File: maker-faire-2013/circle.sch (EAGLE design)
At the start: 11 parts, among them Q1 2N3904, Q2 2N3904

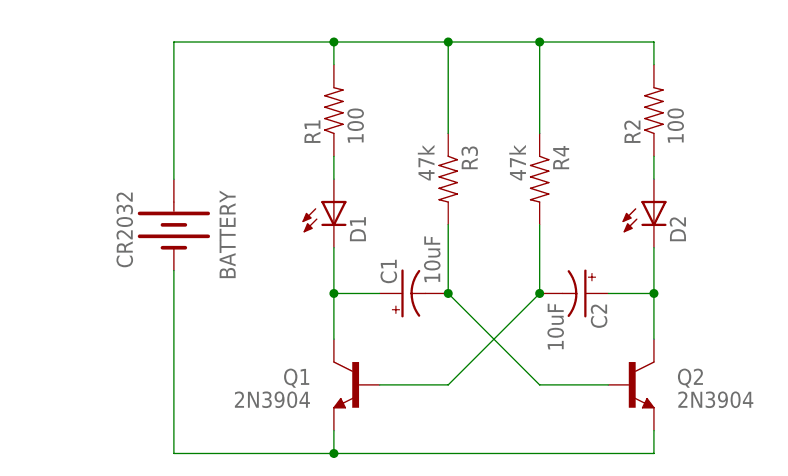
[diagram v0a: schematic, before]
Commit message: Updated with 0.2" caps and power switch
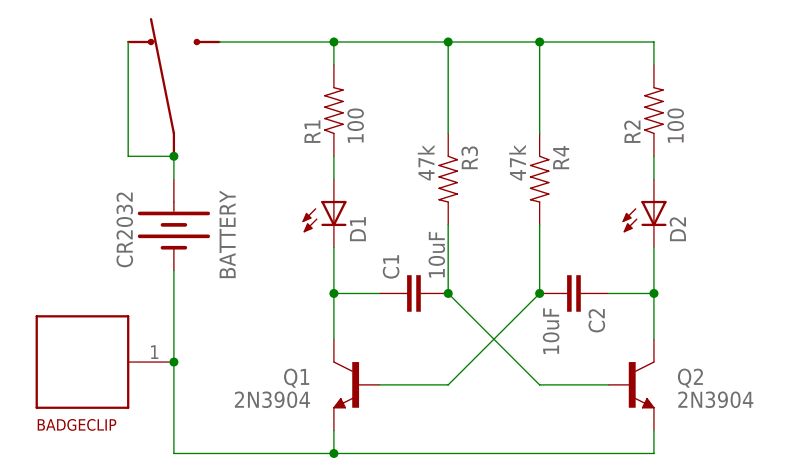
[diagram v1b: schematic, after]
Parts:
- added BADGECLIP: BADGE_CLIP, circle:BADGE_CLIP
- added U$2: 0S102011MS2QN1, circle:0S102011MS2QN1
- BATTERY: device SparkFun-Electromechanical:BATTERY20PTH -> circle:BATTERY20PTH
- C1, C2: device SparkFun-Passives:CAP_POLPTH2 -> circle:C-EU050-024X044
- D1, D2: device SparkFun-LED:LED5MM-KIT -> circle:LED5MM-KIT
- Q1, Q2: device SparkFun-DiscreteSemi:TRANSISTOR_NPNTO-92-AMMO -> circle:TRANSISTOR_NPNTO-92-AMMO
- R1, R2, R3, R4: device SparkFun-Resistors:RESISTORKIT -> circle:RESISTORPTH-1/4W
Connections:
- new net N$1: BATTERY.+, U$2.1, U$2.2
- net GND: now also BADGECLIP.1
- net N$3: now also C2.1; no longer C2.+
- net N$4: now also C1.1; no longer C1.+
- net N$6: now also C2.2; no longer C2.-
- net N$7: now also C1.2; no longer C1.-
- net VCC: now also U$2.3; no longer BATTERY.+

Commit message: Change caps to 0.2 pitch, fix silk issues, panelise into 4 per 10x10 panel
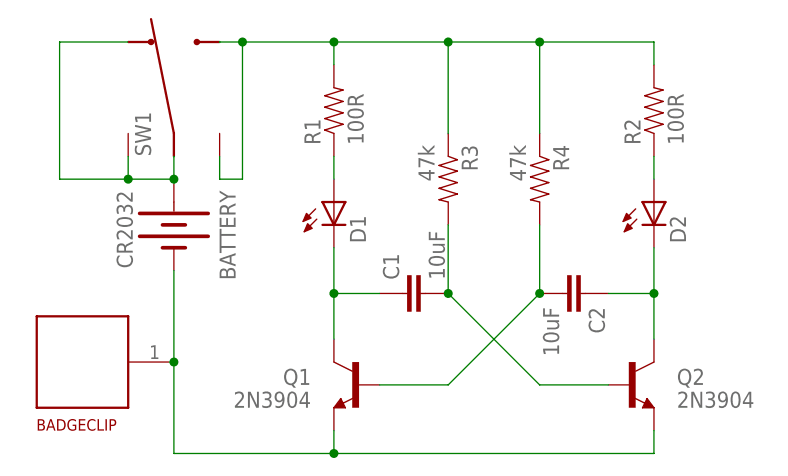
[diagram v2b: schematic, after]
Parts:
- R1, R2: value 100 -> 100R
- renumbered U$2 to SW1
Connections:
- removed net N$1: BATTERY.+, SW1.1, SW1.2
- removed net VCC: R1.2, R2.2, R3.1, R4.1, SW1.3
- new net CASE1: BATTERY.+, SW1.1, SW1.2, SW1.CASE1
- new net CASE2: R1.2, R2.2, R3.1, R4.1, SW1.3, SW1.CASE2

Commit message: 2015 MF PCB final
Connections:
- removed net CASE1: BATTERY.+, SW1.1, SW1.2, SW1.CASE1
- new net N$1: BATTERY.+, SW1.2
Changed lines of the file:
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@@
 <grid distance="0.1" unitdist="inch" unit="inch" style="lines" multiple="1" display="no" altdistance="0.01" altunitdist="inch" altunit="inch"/>
 <layers>
-<layer number="1" name="Top" color="4" fill="1" visible="no" active="no"/>
-<layer number="16" name="Bottom" color="1" fill="1" visible="no" active="no"/>
-<layer number="17" name="Pads" color="2" fill="1" visible="no" active="no"/>
-<layer number="18" name="Vias" color="2" fill="1" visible="no" active="no"/>
-<layer number="19" name="Unrouted" color="6" fill="1" visible="no" active="no"/>
-<layer number="20" name="Dimension" color="15" fill="1" visible="no" active="no"/>
-<layer number="21" name="tPlace" color="7" fill="1" visible="no" active="no"/>
-<layer number="22" name="bPlace" color="7" fill="1" visible="no" active="no"/>
-<layer number="23" name="tOrigins" color="15" fill="1" visible="no" active="no"/>
-<layer number="24" name="bOrigins" color="15" fill="1" visible="no" active="no"/>
-<layer number="25" name="tNames" color="7" fill="1" visible="no" active="no"/>
-<layer number="26" name="bNames" color="7" fill="1" visible="no" active="no"/>
-<layer number="27" name="tValues" color="7" fill="1" visible="no" active="no"/>
-<layer number="28" name="bValues" color="7" fill="1" visible="no" active="no"/>
+<layer number="1" name="Top" color="4" fill="1" visible="yes" active="no"/>
+<layer number="16" name="Bottom" color="1" fill="1" visible="yes" active="no"/>
+<layer number="17" name="Pads" color="2" fill="1" visible="yes" active="no"/>
+<layer number="18" name="Vias" color="2" fill="1" visible="yes" active="no"/>
+<layer number="19" name="Unrouted" color="6" fill="1" visible="yes" active="no"/>
+<layer number="20" name="Dimension" color="15" fill="1" visible="yes" active="no"/>
+<layer number="21" name="tPlace" color="7" fill="1" visible="yes" active="no"/>
+<layer number="22" name="bPlace" color="7" fill="1" visible="yes" active="no"/>
+<layer number="23" name="tOrigins" color="15" fill="1" visible="yes" active="no"/>
+<layer number="24" name="bOrigins" color="15" fill="1" visible="yes" active="no"/>
+<layer number="25" name="tNames" color="7" fill="1" visible="yes" active="no"/>
+<layer number="26" name="bNames" color="7" fill="1" visible="yes" active="no"/>
+<layer number="27" name="tValues" color="7" fill="1" visible="yes" active="no"/>
+<layer number="28" name="bValues" color="7" fill="1" visible="yes" active="no"/>
 <layer number="29" name="tStop" color="7" fill="3" visible="no" active="no"/>
 <layer number="30" name="bStop" color="7" fill="6" visible="no" active="no"/>
@@
 <layer number="35" name="tGlue" color="7" fill="4" visible="no" active="no"/>
 <layer number="36" name="bGlue" color="7" fill="5" visible="no" active="no"/>
-<layer number="37" name="tTest" color="7" fill="1" visible="no" active="no"/>
-<layer number="38" name="bTest" color="7" fill="1" visible="no" active="no"/>
+<layer number="37" name="tTest" color="7" fill="1" visible="yes" active="no"/>
+<layer number="38" name="bTest" color="7" fill="1" visible="yes" active="no"/>
 <layer number="39" name="tKeepout" color="4" fill="11" visible="no" active="no"/>
 <layer number="40" name="bKeepout" color="1" fill="11" visible="no" active="no"/>
@@
 <layer number="44" name="Drills" color="7" fill="1" visible="no" active="no"/>
 <layer number="45" name="Holes" color="7" fill="1" visible="no" active="no"/>
-<layer number="46" name="Milling" color="3" fill="1" visible="no" active="no"/>
-<layer number="47" name="Measures" color="7" fill="1" visible="no" active="no"/>
-<layer number="48" name="Document" color="7" fill="1" visible="no" active="no"/>
-<layer number="49" name="Reference" color="7" fill="1" visible="no" active="no"/>
-<layer number="50" name="dxf" color="7" fill="1" visible="no" active="no"/>
-<layer number="51" name="tDocu" color="7" fill="1" visible="no" active="no"/>
-<layer number="52" name="bDocu" color="7" fill="1" visible="no" active="no"/>
-<layer number="53" name="tGND_GNDA" color="7" fill="9" visible="no" active="no"/>
-<layer number="54" name="bGND_GNDA" color="1" fill="9" visible="no" active="no"/>
-<layer number="56" name="wert" color="7" fill="1" visible="no" active="no"/>
-<layer number="57" name="tCAD" color="7" fill="1" visible="no" active="no"/>
+<layer number="46" name="Milling" color="3" fill="1" visible="yes" active="no"/>
+<layer number="47" name="Measures" color="7" fill="1" visible="yes" active="no"/>
+<layer number="48" name="Document" color="7" fill="1" visible="yes" active="no"/>
+<layer number="49" name="Reference" color="7" fill="1" visible="yes" active="no"/>
+<layer number="50" name="dxf" color="7" fill="1" visible="yes" active="no"/>
+<layer number="51" name="tDocu" color="7" fill="1" visible="yes" active="no"/>
+<layer number="52" name="bDocu" color="7" fill="1" visible="yes" active="no"/>
+<layer number="53" name="tGND_GNDA" color="7" fill="9" visible="yes" active="no"/>
+<layer number="54" name="bGND_GNDA" color="1" fill="9" visible="yes" active="no"/>
+<layer number="56" name="wert" color="7" fill="1" visible="yes" active="no"/>
+<layer number="57" name="tCAD" color="7" fill="1" visible="yes" active="no"/>
 <layer number="90" name="Modules" color="5" fill="1" visible="yes" active="yes"/>
 <layer number="91" name="Nets" color="2" fill="1" visible="yes" active="yes"/>
@@
 </segment>
 </net>
-<net name="CASE1" class="0">
-<segment>
-<pinref part="SW1" gate="G$1" pin="2"/>
-<pinref part="BATTERY" gate="G$1" pin="+"/>
-<pinref part="SW1" gate="G$1" pin="1"/>
-<wire x1="12.7" y1="33.02" x2="12.7" y2="30.48" width="0.1524" layer="91"/>
-<wire x1="12.7" y1="30.48" x2="7.62" y2="30.48" width="0.1524" layer="91"/>
-<wire x1="7.62" y1="30.48" x2="0" y2="30.48" width="0.1524" layer="91"/>
-<wire x1="0" y1="30.48" x2="0" y2="45.72" width="0.1524" layer="91"/>
-<wire x1="0" y1="45.72" x2="7.62" y2="45.72" width="0.1524" layer="91"/>
-<junction x="12.7" y="30.48"/>
-<pinref part="SW1" gate="G$1" pin="CASE1"/>
-<wire x1="7.62" y1="33.02" x2="7.62" y2="30.48" width="0.1524" layer="91"/>
-<junction x="7.62" y="30.48"/>
-</segment>
-</net>
 <net name="CASE2" class="0">
 <segment>
@@
 </segment>
 </net>
+<net name="N$1" class="0">
+<segment>
+<pinref part="BATTERY" gate="G$1" pin="+"/>
+<pinref part="SW1" gate="G$1" pin="2"/>
+<wire x1="12.7" y1="33.02" x2="12.7" y2="30.48" width="0.1524" layer="91"/>
+</segment>
+</net>
